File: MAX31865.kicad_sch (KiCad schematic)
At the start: 22 parts, among them J1 connector, J2 Screw_Terminal_01x04, U1 MAX31865, U2 MIC5225

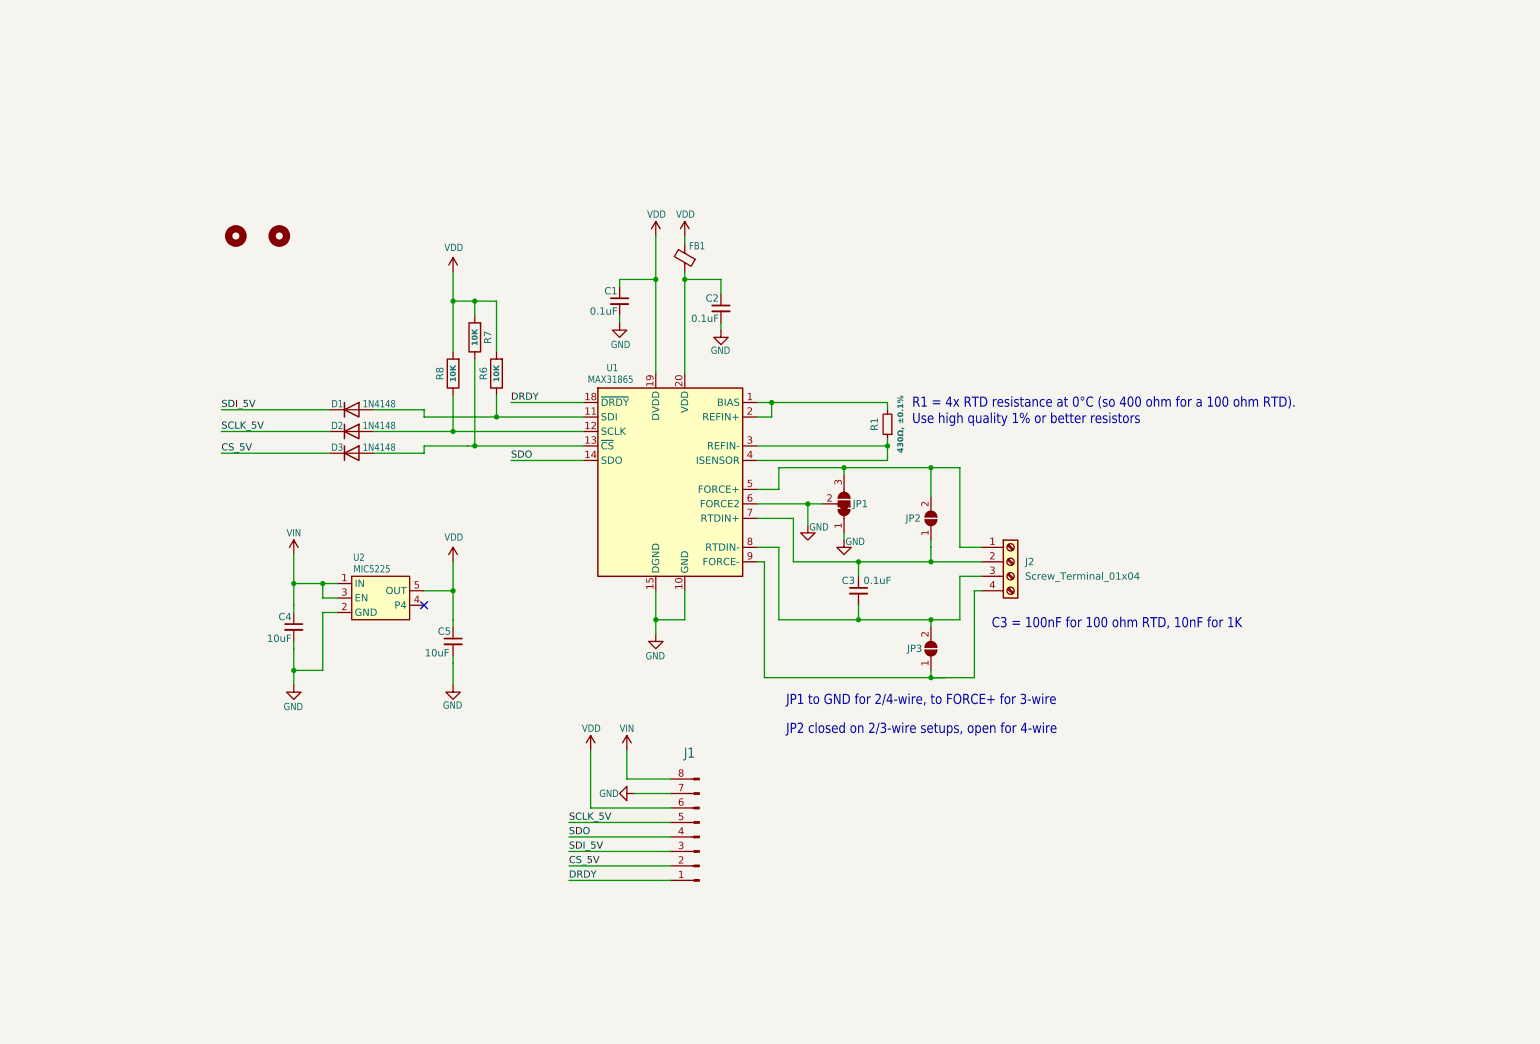
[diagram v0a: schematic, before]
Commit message: Added Nano shield to schematic
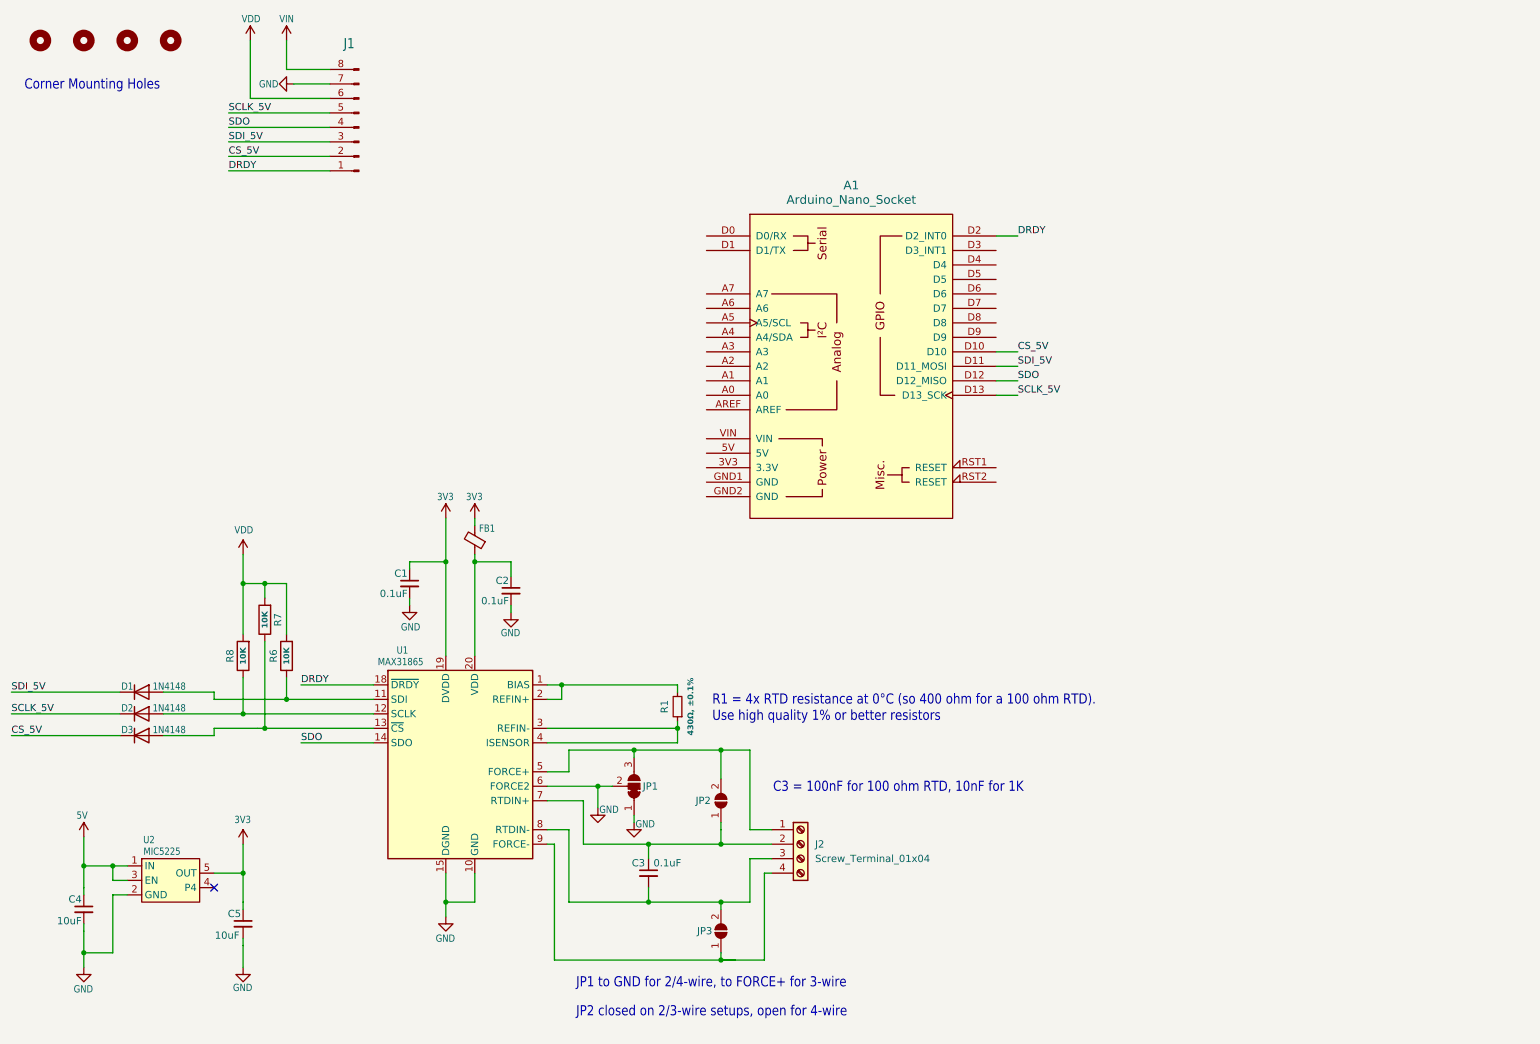
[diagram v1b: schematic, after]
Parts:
- added A1: Arduino_Nano_Socket, PCM_arduino-library:Arduino_Nano_Socket, symbol PCM_arduino-library:Arduino_Nano_Socket
- added U$1, U$2: MOUNTINGHOLE2.5, MountingHole:MountingHole_2.2mm_M2_ISO7380, symbol Mechanical:MountingHole
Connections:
- net CS_5V: now also A1.D10
- net DRDY: now also A1.D2 (D2_INT0)
- net SCLK_5V: now also A1.D13 (D13_SCK)
- net SDI_5V: now also A1.D11 (D11_MOSI)
- net SDO: now also A1.D12 (D12_MISO)
- net VDD: no longer C1.1, C5.1, FB1.2, U1.19 (DVDD), U2.5 (OUT)
- net VIN: no longer C4.1, U2.1 (IN), U2.3 (EN)
- new net 3V3: C1.1, C5.1, FB1.2, U1.19 (DVDD), U2.5 (OUT)
- new net 5V: C4.1, U2.1 (IN), U2.3 (EN)
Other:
- note added: "Corner Mounting Holes"
- company: (none) -> DTU Nanolab
- title: MAX31865 -> RTD Sensor PCB
- moved on the sheet: C1, C2, C3, C4, C5, D1, D2, D3, FB1, J1, J2, JP1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

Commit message: Updated AFE with Arduino shield
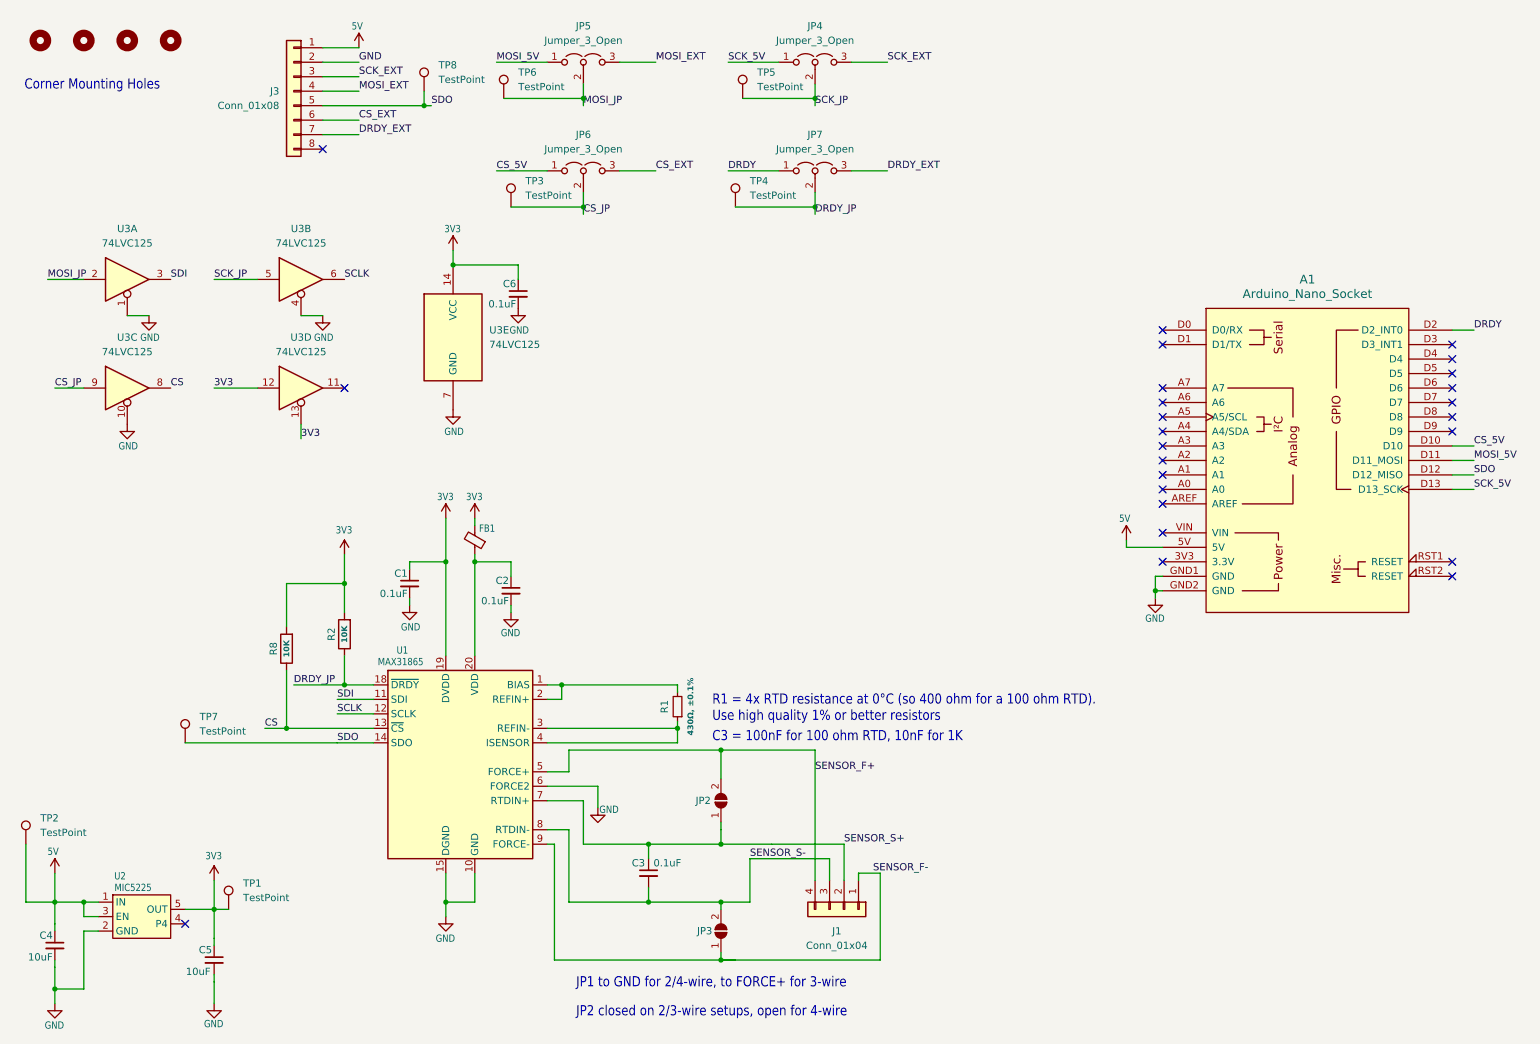
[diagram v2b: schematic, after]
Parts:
- removed D1, D2, D3: 1N4148, Diode_SMD:D_SOD-323, symbol Device:D
- removed J1: connector, Connector_PinHeader_2.54mm:PinHeader_1x08_P2.54mm_Vertical, symbol Connector:Conn_01x08_Pin
- removed J2: Screw_Terminal_01x04, TerminalBlock_4Ucon:TerminalBlock_4Ucon_1x04_P3.50mm_Horizontal, symbol Connector:Screw_Terminal_01x04
- removed JP1: SolderJumper_3_Bridged12, Jumper:SolderJumper-3_P1.3mm_Bridged12_Pad1.0x1.5mm, symbol Jumper:SolderJumper_3_Bridged12
- removed R6, R7: 10K, Resistor_SMD:R_0805_2012Metric, symbol Device:R
- added C6: 0.1uF, Capacitor_SMD:C_0805_2012Metric, symbol Device:C_Small
- added J1: Conn_01x04, SensorFootprint:RTD_Sensor_BondPad_4x, symbol Connector_Generic:Conn_01x04
- added J3: Conn_01x08, Connector_Molex:Molex_KK-254_AE-6410-08A_1x08_P2.54mm_Vertical, symbol Connector_Generic:Conn_01x08
- added JP4, JP5, JP6, JP7: Jumper_3_Open, Connector_PinHeader_2.54mm:PinHeader_1x03_P2.54mm_Vertical, symbol Jumper:Jumper_3_Open
- added R2: 10K, Resistor_SMD:R_0805_2012Metric, symbol Device:R
- added TP1, TP2, TP3, TP4, TP5, TP6, TP7, TP8: TestPoint, TestPoint:TestPoint_Pad_D1.0mm, symbol Connector:TestPoint
- added U3: 74LVC125, Package_SO:TSSOP-14_4.4x5mm_P0.65mm, symbol 74xx:74LVC125
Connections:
- net VDD is gone; now on net 3V3: R8.2
- net 3V3: now also C6.1, R2.2, TP1.1, U3.12, U3.13, U3.14 (VCC)
- net 5V: now also A1.5V, J3.1 (Pin_1), TP2.1
- net CS_5V: now also JP6.1 (A)
- net DRDY: now also JP7.1 (A); no longer U1.18 (~{DRDY})
- net GND: now also A1.GND1 (GND), A1.GND2 (GND), C6.2, J3.2 (Pin_2), U3.1, U3.10, U3.4, U3.7 (GND)
- net SDO: now also J3.5 (Pin_5), TP7.1, TP8.1
- net SENSOR_F-: now reaches JP3.1 (A), U1.9 (FORCE-)
- net SENSOR_F-: now also J1.1 (Pin_1)
- net SENSOR_S-: now reaches C3.2, JP3.2 (B), U1.8 (RTDIN-)
- net SENSOR_S-: now also J1.3 (Pin_3)
- net SENSOR_S+: now reaches C3.1, JP2.1 (A), U1.7 (RTDIN+)
- net SENSOR_S+: now also J1.2 (Pin_2)
- net SENSOR_F+: now reaches JP2.2 (B), U1.5 (FORCE+)
- net SENSOR_F+: now also J1.4 (Pin_4)
- net SDI: now reaches U1.11 (SDI)
- net SDI: now also U3.3
- net CS: now reaches R8.1
- net CS: now also U1.13 (~{CS}), U3.8; no longer U1.12 (SCLK)
- net SCLK_5V renamed SCK_5V
- net SCK_5V: now also JP4.1 (A)
- net SDI_5V renamed MOSI_5V
- net MOSI_5V: now also JP5.1 (A)
- new net CS_EXT: J3.6 (Pin_6), JP6.3 (B)
- new net CS_JP: JP6.2 (C), TP3.1, U3.9
- new net DRDY_EXT: J3.7 (Pin_7), JP7.3 (B)
- new net DRDY_JP: JP7.2 (C), R2.1, TP4.1, U1.18 (~{DRDY})
- new net MOSI_EXT: J3.4 (Pin_4), JP5.3 (B)
- new net MOSI_JP: JP5.2 (C), TP6.1, U3.2
- new net SCK_EXT: J3.3 (Pin_3), JP4.3 (B)
- new net SCK_JP: JP4.2 (C), TP5.1, U3.5
- new net SCLK: U1.12 (SCLK), U3.6
- no-connect marks 1 -> 25
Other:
- moved on the sheet: A1, C4, C5, R8, U2

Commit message: Updated sensor footprint
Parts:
- removed TP8: TestPoint, TestPoint:TestPoint_Pad_D1.0mm, symbol Connector:TestPoint
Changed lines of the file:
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@@
-	)
-	(junction
-		(at 86.36 29.21)
-		(diameter 0)
-		(color 0 0 0 0)
 	)
 	(junction
@@
 	(wire
 		(pts
-			(xy 86.36 26.67) (xy 86.36 29.21)
-		)
-		(stroke
-			(width 0)
-			(type default)
-		)
-	)
-	(wire
-		(pts
 			(xy 95.25 107.95) (xy 95.25 109.22)
 		)
@@
 	(wire
 		(pts
-			(xy 68.58 29.21) (xy 86.36 29.21)
+			(xy 68.58 29.21) (xy 74.93 29.21)
 		)
 		(stroke
@@
 		(pts
 			(xy 49.53 78.74) (xy 57.15 78.74)
-		)
-		(stroke
-			(width 0)
-			(type default)
-		)
-	)
-	(wire
-		(pts
-			(xy 86.36 29.21) (xy 87.63 29.21)
 		)
 		(stroke
@@
 	)
 	(label "SDO"
-		(at 87.63 29.21 0)
+		(at 74.93 29.21 0)
 		(effects
 			(font
@@
 					(unit 1)
 				)
-			)
-		)
-	)
-	(symbol
-		(lib_id "Connector:TestPoint")
-		(at 86.36 26.67 0)
-		(unit 1)
-		(exclude_from_sim no)
-		(in_bom yes)
-		(on_board yes)
-		(dnp no)
-		(fields_autoplaced yes)
-		(property "Reference" "TP8"
-			(at 88.9 22.0979 0)
-			(effects
-				(font
-					(size 1.27 1.27)
-				)
-				(justify left)
-			)
-		)
-		(property "Value" "TestPoint"
-			(at 88.9 24.6379 0)
-			(effects
-				(font
-					(size 1.27 1.27)
-				)
-				(justify left)
-			)
-		)
-		(property "Footprint" "TestPoint:TestPoint_Pad_D1.0mm"
-			(at 91.44 26.67 0)
-			(effects
-				(font
-					(size 1.27 1.27)
-				)
-				(hide yes)
-			)
-		)
-		(property "Datasheet" "~"
-			(at 91.44 26.67 0)
-			(effects
-				(font
-					(size 1.27 1.27)
-				)
-				(hide yes)
-			)
-		)
-		(property "Description" "test point"
-			(at 86.36 26.67 0)
-			(effects
-				(font
-					(size 1.27 1.27)
-				)
-				(hide yes)
-			)
-		)
-		(pin "1"
-		)
-		(instances
-			(project "MAX31865"
-				(path "/7d3dfe06-ad22-4135-8721-3b06d69e4560"
-					(reference "TP8")
-					(unit 1)
-				)

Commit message: planed supply rails
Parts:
- added C7: 10uF, Capacitor_SMD:C_0805_2012Metric, symbol Device:C_Small
- added R3: 0ohm, Resistor_SMD:R_0805_2012Metric, symbol PCM_SL_Resistors:0ohm
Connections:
- net GND: now also R3.1; no longer C2.2, U1.10 (GND), U1.16 (GND), U1.21 (GND), U1.6 (FORCE2)
- net SENSOR_F+: now also J1.2 (Pin_2); no longer J1.4 (Pin_4)
- net SENSOR_F-: now also J1.3 (Pin_3); no longer J1.1 (Pin_1)
- net SENSOR_S+: now also J1.4 (Pin_4); no longer J1.2 (Pin_2)
- net SENSOR_S-: now also J1.1 (Pin_1); no longer J1.3 (Pin_3)
- net at C2.1, FB1.1, U1.20 (VDD): now also C7.1
- new net GNDA: C2.2, C7.2, R3.2, U1.10 (GND), U1.16 (GND), U1.21 (GND), U1.6 (FORCE2)
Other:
- moved on the sheet: J1

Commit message: Cleaned up footprint library
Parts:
- FB1: footprint external_footprints:LI0805G201R-10 -> footprints:LI0805G201R-10
- J1: footprint SensorFootprint:RTD_Sensor_BondPad_4x -> footprints:RTD_Sensor_BondPad_4x
- U1: footprint external_footprints:MAX31865ATP+ -> footprints:MAX31865ATP+
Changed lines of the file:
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@@
 			)
 		)
-		(property "Footprint" "external_footprints:MAX31865ATP+"
+		(property "Footprint" "footprints:MAX31865ATP+"
 			(at 96.52 162.56 0)
 			(effects
@@
 			)
 		)
-		(property "Footprint" "external_footprints:LI0805G201R-10"
+		(property "Footprint" "footprints:LI0805G201R-10"
 			(at 97.028 105.41 90)
 			(effects
@@
 			)
 		)
-		(property "Footprint" "SensorFootprint:RTD_Sensor_BondPad_4x"
+		(property "Footprint" "footprints:RTD_Sensor_BondPad_4x"
 			(at 163.83 148.59 0)
 			(effects

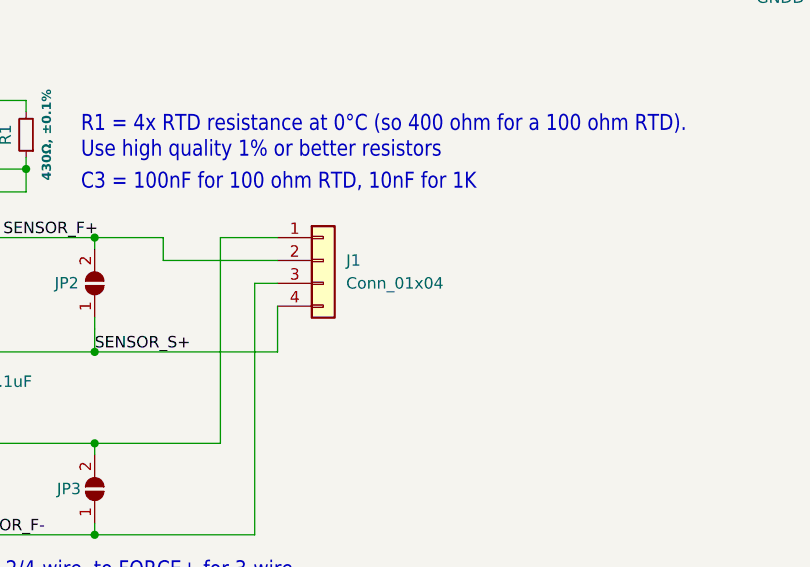
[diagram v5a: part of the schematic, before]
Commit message: collected external syms and footprints
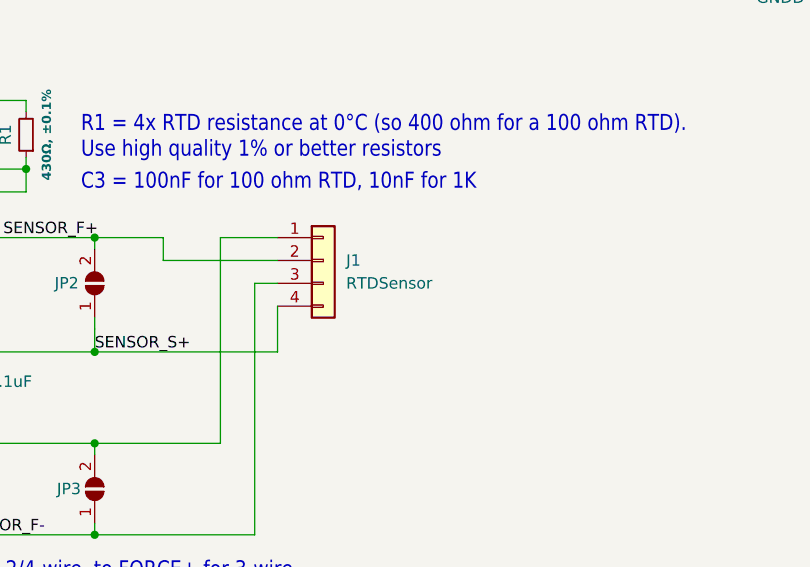
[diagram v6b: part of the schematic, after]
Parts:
- A1: footprint PCM_arduino-library:Arduino_Nano_Socket -> external_footprints:Arduino_Nano_Socket
- FB1: footprint footprints:LI0805G201R-10 -> external_footprints:LI0805G201R-10
- J1: value Conn_01x04 -> RTDSensor; footprint footprints:RTD_Sensor_BondPad_4x -> external_footprints:RTD_Sensor_BondPad_4x
- U1: footprint footprints:MAX31865ATP+ -> external_footprints:MAX31865ATP+
- U2: footprint Package_TO_SOT_SMD:SOT-23-5 -> external_footprints:MIC5225
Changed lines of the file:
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@@
 			)
 		)
-		(property "Footprint" "Package_TO_SOT_SMD:SOT-23-5"
+		(property "Footprint" "external_footprints:MIC5225"
 			(at 31.75 176.53 0)
 			(effects
@@
 			)
 		)
-		(property "Footprint" "footprints:MAX31865ATP+"
+		(property "Footprint" "external_footprints:MAX31865ATP+"
 			(at 96.52 162.56 0)
 			(effects
@@
 			)
 		)
-		(property "Footprint" "PCM_arduino-library:Arduino_Nano_Socket"
+		(property "Footprint" "external_footprints:Arduino_Nano_Socket"
 			(at 241.3 125.73 0)
 			(effects
@@
 			)
 		)
-		(property "Footprint" "footprints:LI0805G201R-10"
+		(property "Footprint" "external_footprints:LI0805G201R-10"
 			(at 97.028 105.41 90)
 			(effects
@@
 			)
 		)
-		(property "Value" "Conn_01x04"
+		(property "Value" "RTDSensor"
 			(at 166.37 151.1299 0)
 			(effects
@@
 			)
 		)
-		(property "Footprint" "footprints:RTD_Sensor_BondPad_4x"
+		(property "Footprint" "external_footprints:RTD_Sensor_BondPad_4x"
 			(at 163.83 148.59 0)
 			(effects

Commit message: ci external cleanup
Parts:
- U3: footprint Package_SO:TSSOP-14_4.4x5mm_P0.65mm -> external_footprints:74LVC125
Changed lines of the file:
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@@
 			)
 		)
-		(property "Footprint" "Package_SO:TSSOP-14_4.4x5mm_P0.65mm"
+		(property "Footprint" "external_footprints:74LVC125"
 			(at 34.29 59.69 0)
 			(effects
@@
 			)
 		)
-		(property "Footprint" "Package_SO:TSSOP-14_4.4x5mm_P0.65mm"
+		(property "Footprint" "external_footprints:74LVC125"
 			(at 34.29 78.74 0)
 			(effects
@@
 			)
 		)
-		(property "Footprint" "Package_SO:TSSOP-14_4.4x5mm_P0.65mm"
+		(property "Footprint" "external_footprints:74LVC125"
 			(at 64.77 59.69 0)
 			(effects
@@
 			)
 		)
-		(property "Footprint" "Package_SO:TSSOP-14_4.4x5mm_P0.65mm"
+		(property "Footprint" "external_footprints:74LVC125"
 			(at 64.77 78.74 0)
 			(effects
@@
 			)
 		)
-		(property "Footprint" "Package_SO:TSSOP-14_4.4x5mm_P0.65mm"
+		(property "Footprint" "external_footprints:74LVC125"
 			(at 91.44 69.85 0)
 			(effects
